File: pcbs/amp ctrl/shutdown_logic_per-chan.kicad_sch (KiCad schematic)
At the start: 24 parts, among them U17 74LVC2G17, U4 74HC02, U5 74LVC2G06

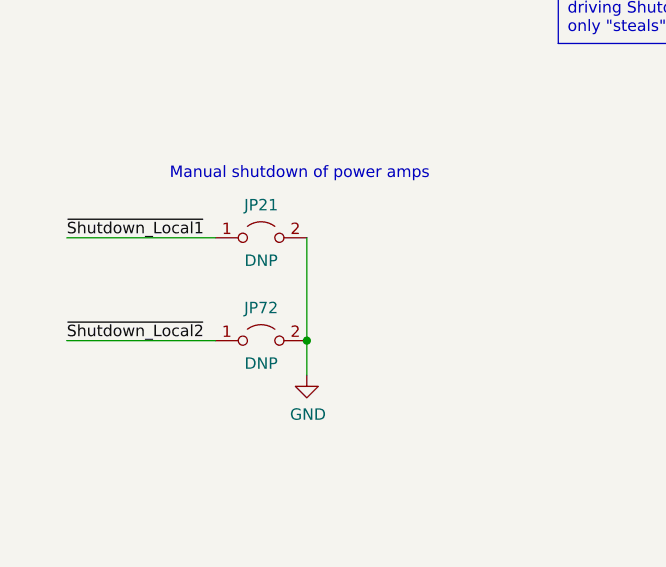
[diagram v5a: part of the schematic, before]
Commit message: Misc. cleanup for mfg & improvements
Minor backplane pinout doc corrections (SCKO5 polarity, clarified some descriptions)
Backplane: Added differential- and common-mode (to standoffs) power filtering, for EMI escaping over power wiring
Amp ctrl: Changed DAC testpoints from individual pads to Keystone 5019 for easier probing
Corrected part numbers, DNP vs. non-BOM-item indications, other misc. BOM issues
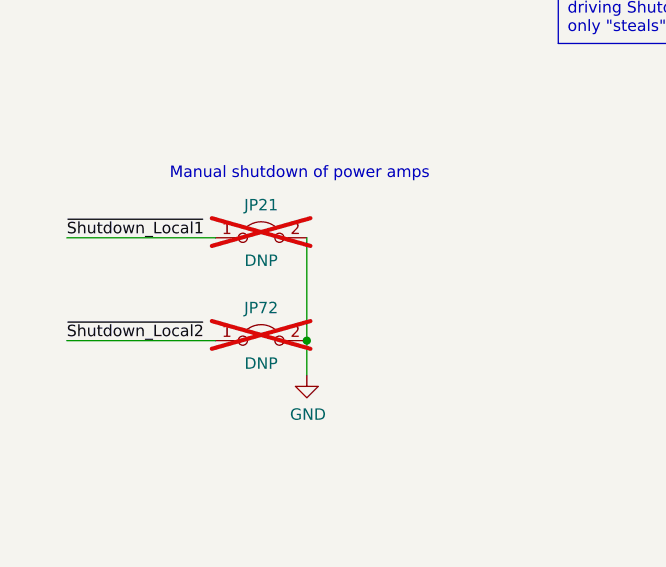
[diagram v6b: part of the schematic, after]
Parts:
- JP21, JP72: now not fitted; now left out of the parts list
- TP11, TP12, TP14, TP140, TP15, TP7: now left out of the parts list
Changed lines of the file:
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@@
 		(unit 1)
 		(exclude_from_sim no)
-		(in_bom yes)
+		(in_bom no)
 		(on_board yes)
 		(dnp no)
@@
 		(unit 1)
 		(exclude_from_sim no)
-		(in_bom yes)
+		(in_bom no)
 		(on_board yes)
 		(dnp no)
@@
 		(unit 1)
 		(exclude_from_sim no)
-		(in_bom yes)
+		(in_bom no)
 		(on_board yes)
 		(dnp no)
@@
 		(unit 1)
 		(exclude_from_sim no)
-		(in_bom yes)
+		(in_bom no)
 		(on_board yes)
 		(dnp no)
@@
 		(unit 1)
 		(exclude_from_sim no)
-		(in_bom yes)
+		(in_bom no)
 		(on_board yes)
-		(dnp no)
+		(dnp yes)
 		(property "Reference" "JP21"
 			(at 68.58 150.0378 0)
@@
 		(unit 1)
 		(exclude_from_sim no)
-		(in_bom yes)
+		(in_bom no)
 		(on_board yes)
 		(dnp no)
@@
 		(unit 1)
 		(exclude_from_sim no)
-		(in_bom yes)
+		(in_bom no)
 		(on_board yes)
 		(dnp no)
@@
 		(unit 1)
 		(exclude_from_sim no)
-		(in_bom yes)
+		(in_bom no)
 		(on_board yes)
-		(dnp no)
+		(dnp yes)
 		(property "Reference" "JP72"
 			(at 68.58 161.4678 0)

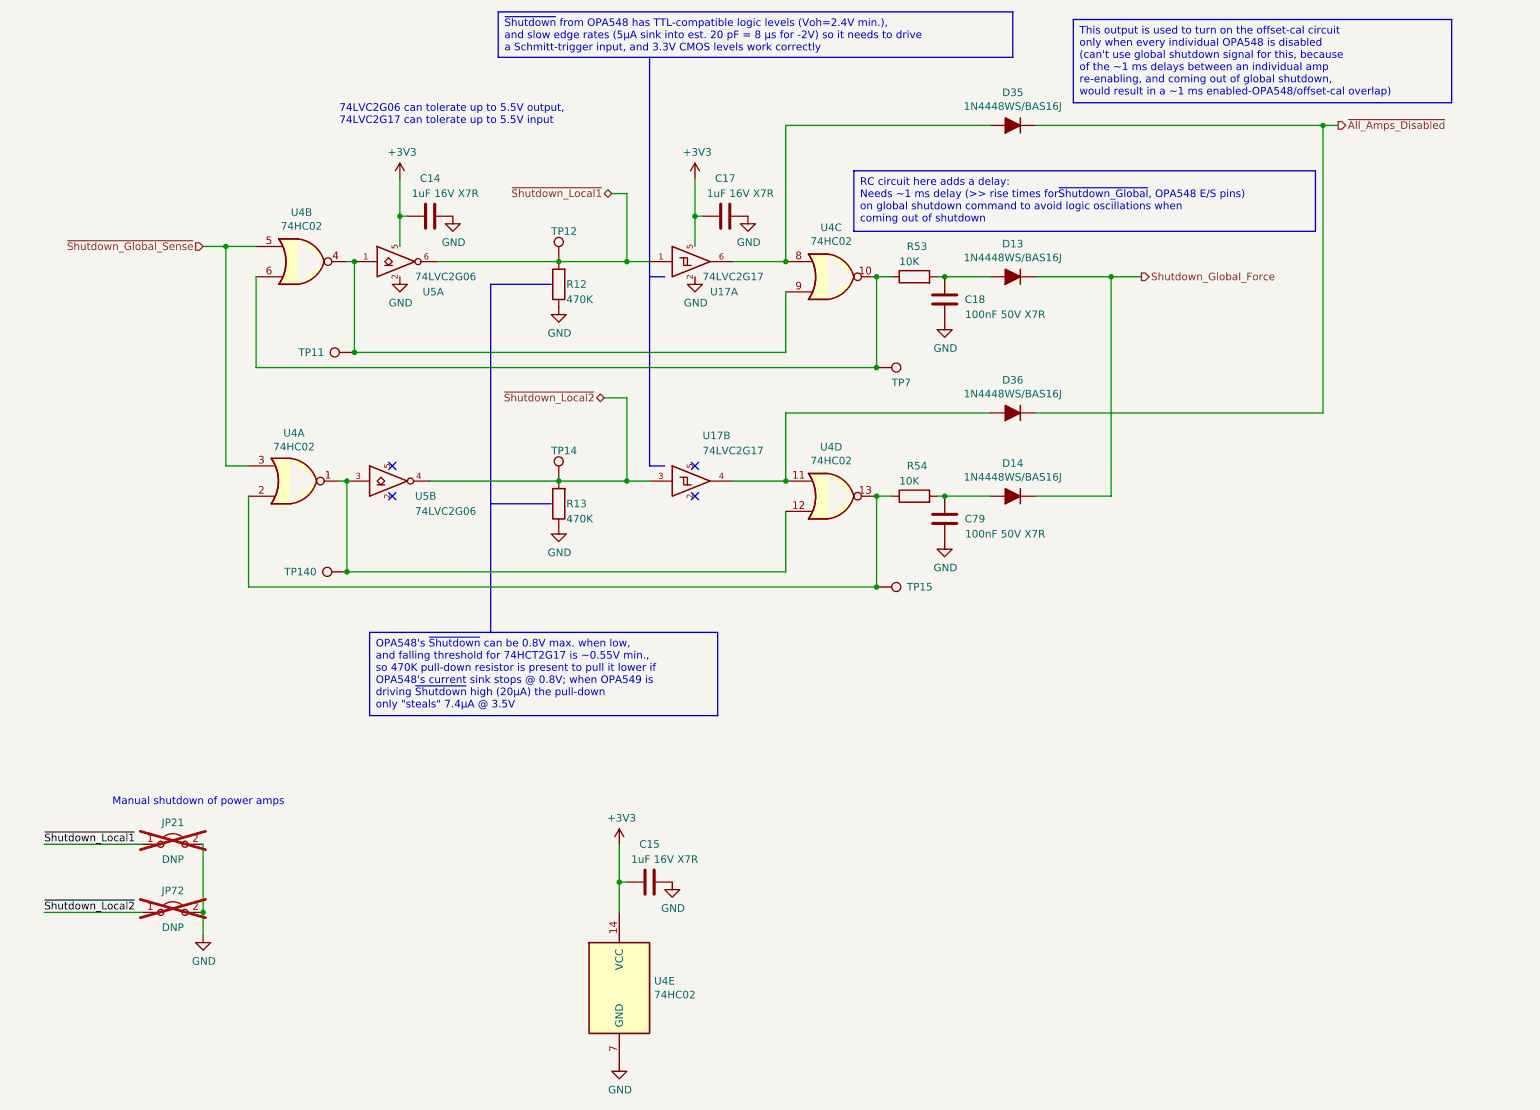
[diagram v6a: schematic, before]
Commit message: Updated KiCAD file versions to 9.0
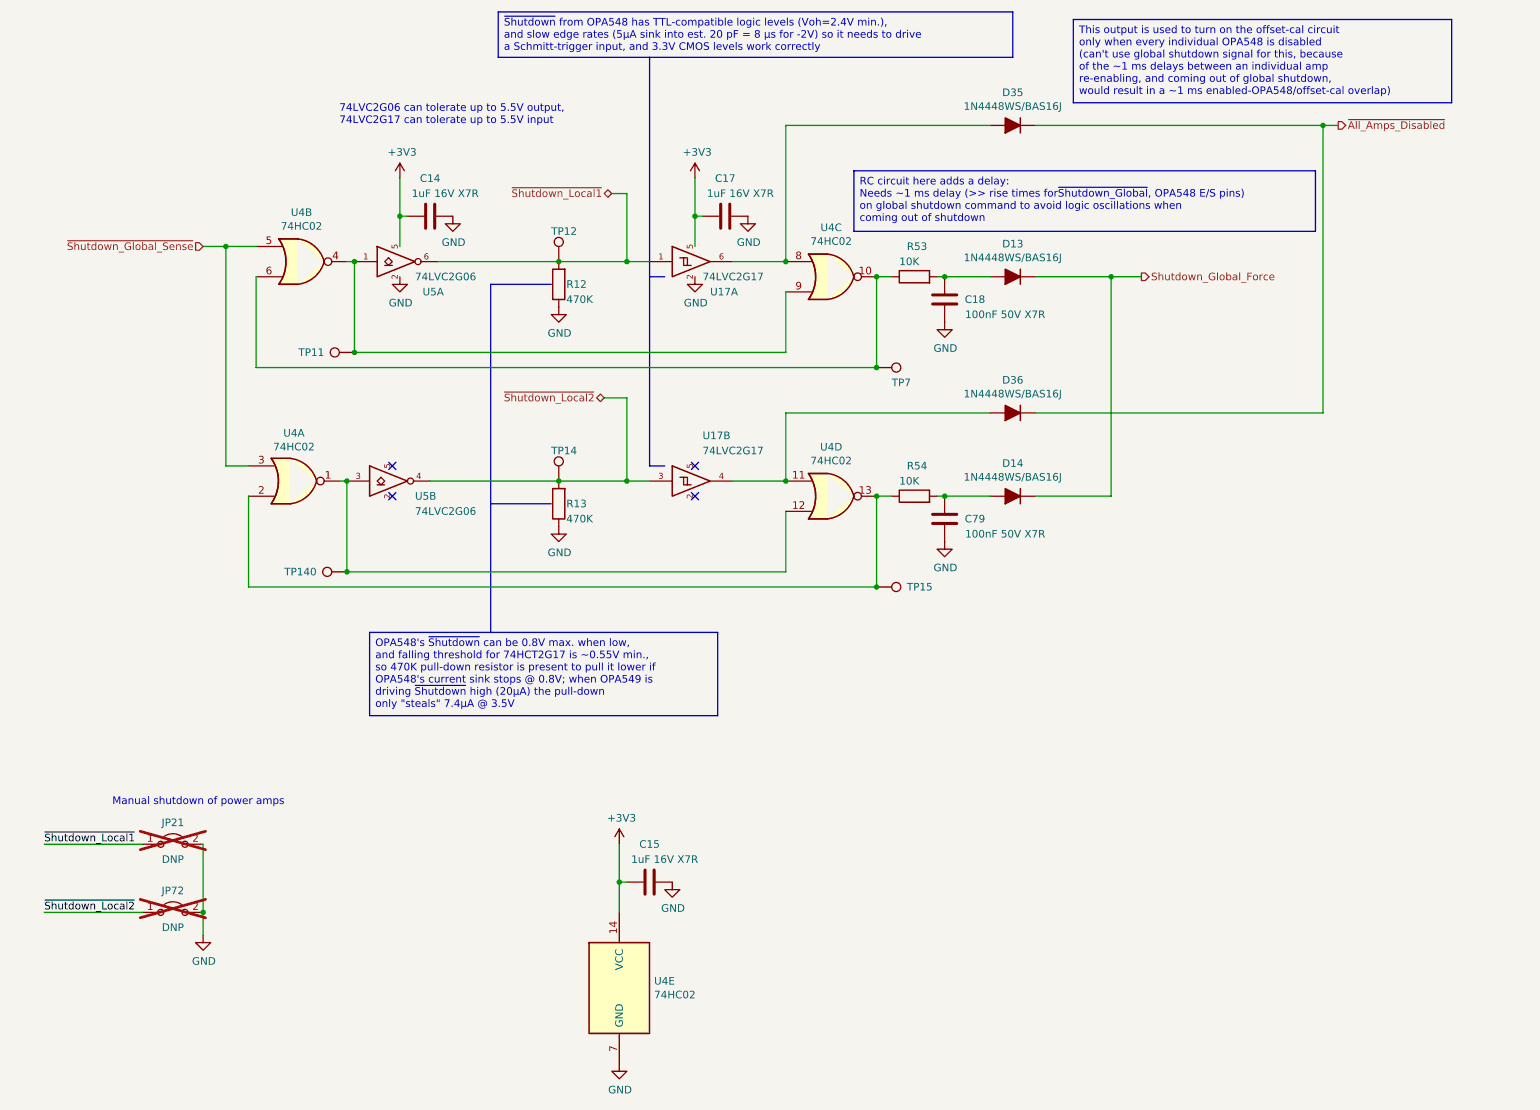
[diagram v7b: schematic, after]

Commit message: Moved all project-specific symbols & footprints into new "shim" libraries Updated projects to reference the new "shim" library
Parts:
- D13, D14, D35, D36: footprint Don_std:D_SOD-323F -> shim:D_SOD-323F
- U17, U5: footprint Martinos_std:SOT-23-6 -> Package_TO_SOT_SMD:SOT-23-6
- U4: footprint Martinos_std:TSSOP-14_4.4x5mm_P0.65mm -> Package_SO:TSSOP-14_4.4x5mm_P0.65mm
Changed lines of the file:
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@@
 			)
 		)
-		(property "Footprint" "Martinos_std:SOT-23-6"
+		(property "Footprint" "Package_TO_SOT_SMD:SOT-23-6"
 			(at 105.41 92.71 0)
 			(effects
@@
 			)
 		)
-		(property "Footprint" "Martinos_std:SOT-23-6"
+		(property "Footprint" "Package_TO_SOT_SMD:SOT-23-6"
 			(at 156.21 92.71 0)
 			(effects
@@
 			)
 		)
-		(property "Footprint" "Martinos_std:SOT-23-6"
+		(property "Footprint" "Package_TO_SOT_SMD:SOT-23-6"
 			(at 156.21 55.88 0)
 			(effects
@@
 			)
 		)
-		(property "Footprint" "Martinos_std:TSSOP-14_4.4x5mm_P0.65mm"
+		(property "Footprint" "Package_SO:TSSOP-14_4.4x5mm_P0.65mm"
 			(at 88.9 92.71 0)
 			(effects
@@
 			)
 		)
-		(property "Footprint" "Martinos_std:TSSOP-14_4.4x5mm_P0.65mm"
+		(property "Footprint" "Package_SO:TSSOP-14_4.4x5mm_P0.65mm"
 			(at 90.17 55.88 0)
 			(effects
@@
 			)
 		)
-		(property "Footprint" "Martinos_std:TSSOP-14_4.4x5mm_P0.65mm"
+		(property "Footprint" "Package_SO:TSSOP-14_4.4x5mm_P0.65mm"
 			(at 179.07 58.42 0)
 			(effects
@@
 			)
 		)
-		(property "Footprint" "Martinos_std:TSSOP-14_4.4x5mm_P0.65mm"
+		(property "Footprint" "Package_SO:TSSOP-14_4.4x5mm_P0.65mm"
 			(at 179.07 95.25 0)
 			(effects
@@
 			)
 		)
-		(property "Footprint" "Martinos_std:TSSOP-14_4.4x5mm_P0.65mm"
+		(property "Footprint" "Package_SO:TSSOP-14_4.4x5mm_P0.65mm"
 			(at 143.51 177.8 0)
 			(effects
@@
 			)
 		)
-		(property "Footprint" "Martinos_std:SOT-23-6"
+		(property "Footprint" "Package_TO_SOT_SMD:SOT-23-6"
 			(at 106.68 55.88 0)
 			(effects
@@
 			)
 		)
-		(property "Footprint" "Don_std:D_SOD-323F"
+		(property "Footprint" "shim:D_SOD-323F"
 			(at 209.55 58.42 0)
 			(effects
@@
 			)
 		)
-		(property "Footprint" "Don_std:D_SOD-323F"
+		(property "Footprint" "shim:D_SOD-323F"
 			(at 209.55 95.25 0)
 			(effects
@@
 			)
 		)
-		(property "Footprint" "Don_std:D_SOD-323F"
+		(property "Footprint" "shim:D_SOD-323F"
 			(at 209.55 33.02 0)
 			(effects
@@
 			)
 		)
-		(property "Footprint" "Don_std:D_SOD-323F"
+		(property "Footprint" "shim:D_SOD-323F"
 			(at 209.55 81.28 0)
 			(effects
